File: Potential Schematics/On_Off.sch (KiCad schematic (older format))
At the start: 7 parts

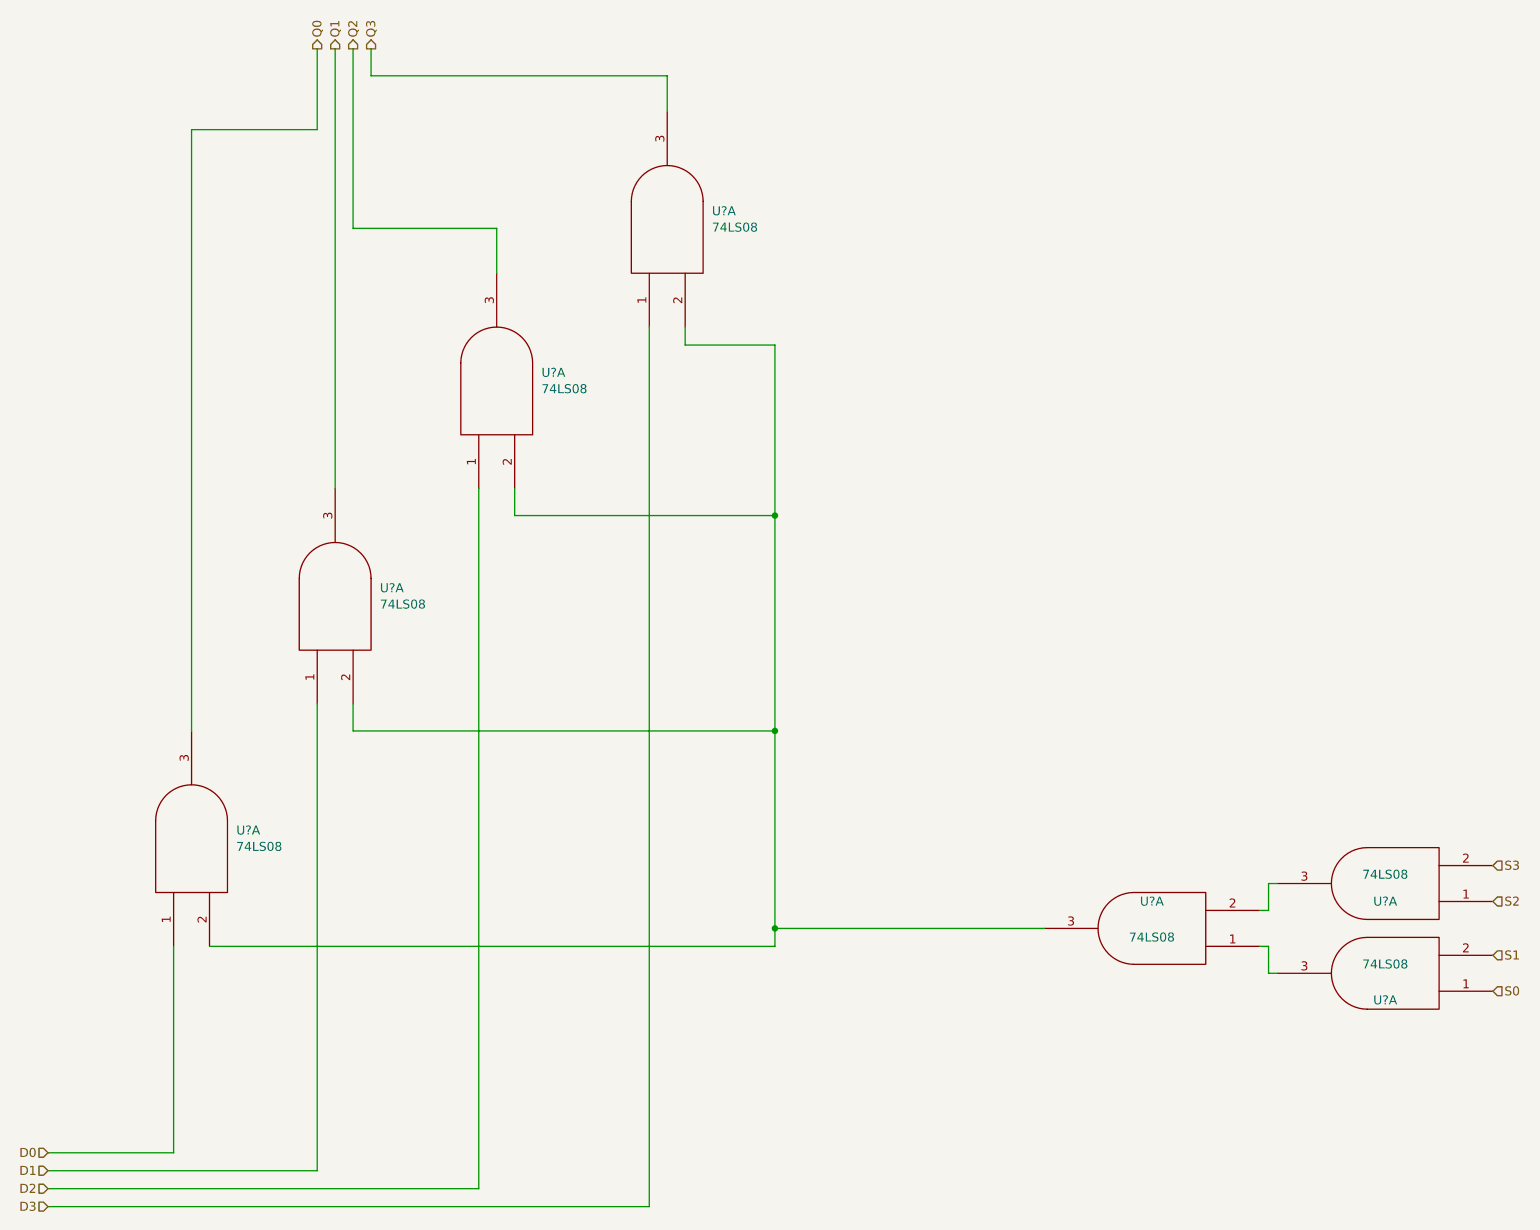
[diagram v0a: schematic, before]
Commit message: Updated overview of Schematic
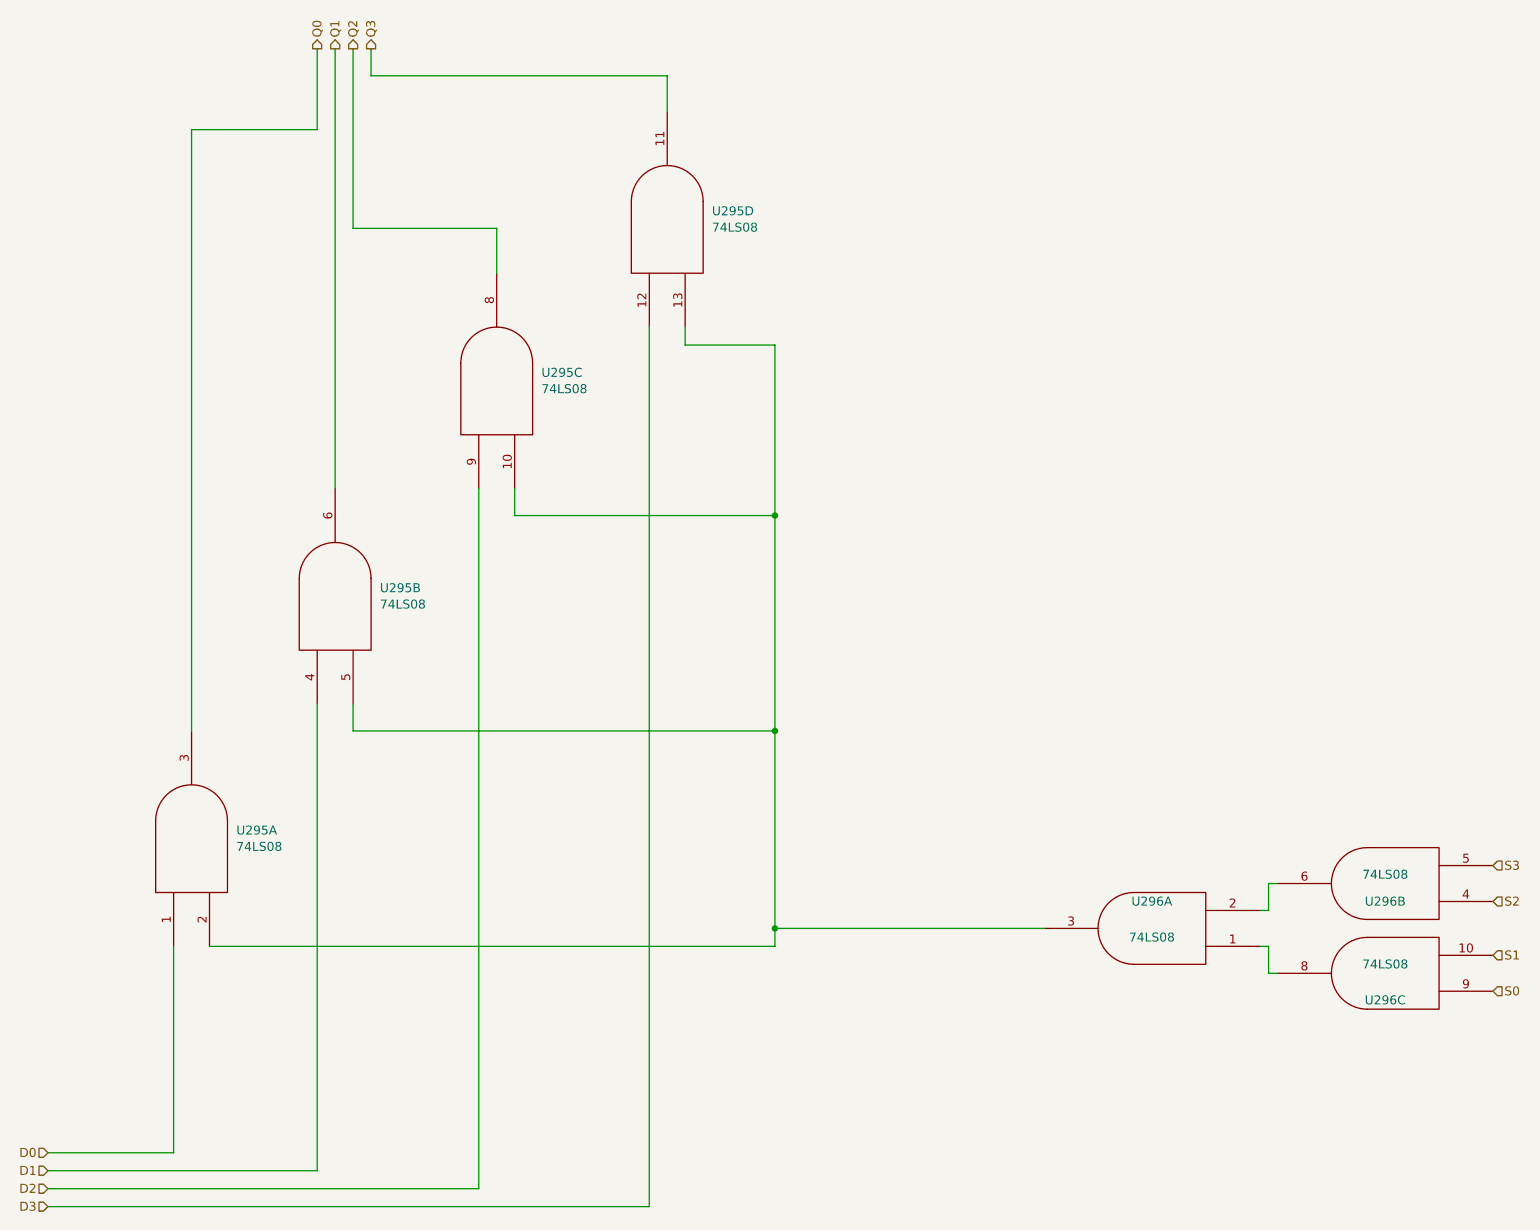
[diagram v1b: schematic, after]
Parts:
- gave numbers to parts that had none: 3
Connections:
- net D1: now also U28.4; no longer U28.1
- net D2: now also U292.9; no longer U292.1
- net D3: now also U292.12; no longer U292.1
- net Q1: now also U28.6; no longer U28.3
- net Q2: now also U292.8; no longer U292.3
- net Q3: now also U292.11; no longer U292.3
- net S0: now also U293.9; no longer U293.1
- net S1: now also U293.10; no longer U293.2
- net S2: now also U292.4; no longer U292.1
- net S3: now also U292.5; no longer U292.2
- net at U292.2: now also U292.6; no longer U292.3
- net at U292.1: now also U293.8; no longer U293.3
- new net: U28.2, U28.5, U292.10, U292.13, U292.3
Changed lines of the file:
@@
 $Descr A4 11693 8268
 encoding utf-8
-Sheet 452 467
+Sheet 452 902
 Title ""
 Date ""
@@
 Q3
 $Comp
-L 4-bit_processor-rescue:74LS08 U?
-U 1 1 5BB2D915
+L 4-bit_processor-rescue:74LS08 U292
+U 2 1 5BB2D915
 P 8900 5700
-F 0 "U?" H 8900 5800 50  0000 C CNN
+AR Path="/5B9D167A/5BAA33A0/5BAA651A/5BB2D6F7/5BB2D915" Ref="U292"  Part="4"
+AR Path="/5B9D167A/5BAA33A0/5BAA651A/5BB302D5/5BB2D915" Ref="U294"  Part="3"
+AR Path="/5B9D167A/5BAA33A0/5BAA651A/5BB303BB/5BB2D915" Ref="U296"  Part="2"
+F 0 "U296" H 8900 5800 50  0000 C CNN
 F 1 "74LS08" H 8900 5650 50  0000 C CNN
 F 2 "" H 8900 5700 50  0001 C CNN
 F 3 "" H 8900 5700 50  0001 C CNN
-	1    8900 5700
+	2    8900 5700
 	-1   0    0    1
 $EndComp
 $Comp
-L 4-bit_processor-rescue:74LS08 U?
-U 1 1 5BB2D984
+L 4-bit_processor-rescue:74LS08 U293
+U 3 1 5BB2D984
 P 8900 6200
-F 0 "U?" H 8900 6350 50  0000 C CNN
+AR Path="/5B9D167A/5BAA33A0/5BAA651A/5BB2D6F7/5BB2D984" Ref="U293"  Part="1"
+AR Path="/5B9D167A/5BAA33A0/5BAA651A/5BB302D5/5BB2D984" Ref="U294"  Part="4"
+AR Path="/5B9D167A/5BAA33A0/5BAA651A/5BB303BB/5BB2D984" Ref="U296"  Part="3"
+F 0 "U296" H 8900 6350 50  0000 C CNN
 F 1 "74LS08" H 8900 6150 50  0000 C CNN
 F 2 "" H 8900 6200 50  0001 C CNN
 F 3 "" H 8900 6200 50  0001 C CNN
-	1    8900 6200
+	3    8900 6200
 	-1   0    0    1
 $EndComp
 $Comp
-L 4-bit_processor-rescue:74LS08 U?
+L 4-bit_processor-rescue:74LS08 U292
 U 1 1 5BB2DA56
 P 7600 5950
-F 0 "U?" H 7600 5800 50  0000 C CNN
+AR Path="/5B9D167A/5BAA33A0/5BAA651A/5BB2D6F7/5BB2DA56" Ref="U292"  Part="3"
+AR Path="/5B9D167A/5BAA33A0/5BAA651A/5BB302D5/5BB2DA56" Ref="U294"  Part="2"
+AR Path="/5B9D167A/5BAA33A0/5BAA651A/5BB303BB/5BB2DA56" Ref="U296"  Part="1"
+F 0 "U296" H 7600 5800 50  0000 C CNN
 F 1 "74LS08" H 7600 6000 50  0000 C CNN
 F 2 "" H 7600 5950 50  0001 C CNN
@@
 	8250 6200 8300 6200
 $Comp
-L 4-bit_processor-rescue:74LS08 U?
+L 4-bit_processor-rescue:74LS08 U28
 U 1 1 5BB2DBA4
 P 2250 5450
-F 0 "U?" V 2296 5201 50  0000 R CNN
+AR Path="/5B9D167A/5BAA33A0/5BAA651A/5BB2D6F7/5BB2DBA4" Ref="U28"  Part="3"
+AR Path="/5B9D167A/5BAA33A0/5BAA651A/5BB302D5/5BB2DBA4" Ref="U293"  Part="2"
+AR Path="/5B9D167A/5BAA33A0/5BAA651A/5BB303BB/5BB2DBA4" Ref="U295"  Part="1"
+F 0 "U295" V 2296 5201 50  0000 R CNN
 F 1 "74LS08" V 2205 5201 50  0000 R CNN
 F 2 "" H 2250 5450 50  0001 C CNN
@@
 $EndComp
 $Comp
-L 4-bit_processor-rescue:74LS08 U?
-U 1 1 5BB2DEAF
+L 4-bit_processor-rescue:74LS08 U28
+U 2 1 5BB2DEAF
 P 3050 4100
-F 0 "U?" V 3096 3851 50  0000 R CNN
+AR Path="/5B9D167A/5BAA33A0/5BAA651A/5BB2D6F7/5BB2DEAF" Ref="U28"  Part="4"
+AR Path="/5B9D167A/5BAA33A0/5BAA651A/5BB302D5/5BB2DEAF" Ref="U293"  Part="3"
+AR Path="/5B9D167A/5BAA33A0/5BAA651A/5BB303BB/5BB2DEAF" Ref="U295"  Part="2"
+F 0 "U295" V 3096 3851 50  0000 R CNN
 F 1 "74LS08" V 3005 3851 50  0000 R CNN
 F 2 "" H 3050 4100 50  0001 C CNN
 F 3 "" H 3050 4100 50  0001 C CNN
-	1    3050 4100
+	2    3050 4100
 	0    -1   -1   0
 $EndComp
 $Comp
-L 4-bit_processor-rescue:74LS08 U?
-U 1 1 5BB2DF82
+L 4-bit_processor-rescue:74LS08 U292
+U 3 1 5BB2DF82
 P 3950 2900
-F 0 "U?" V 3996 2651 50  0000 R CNN
+AR Path="/5B9D167A/5BAA33A0/5BAA651A/5BB2D6F7/5BB2DF82" Ref="U292"  Part="1"
+AR Path="/5B9D167A/5BAA33A0/5BAA651A/5BB302D5/5BB2DF82" Ref="U293"  Part="4"
+AR Path="/5B9D167A/5BAA33A0/5BAA651A/5BB303BB/5BB2DF82" Ref="U295"  Part="3"
+F 0 "U295" V 3996 2651 50  0000 R CNN
 F 1 "74LS08" V 3905 2651 50  0000 R CNN
 F 2 "" H 3950 2900 50  0001 C CNN
 F 3 "" H 3950 2900 50  0001 C CNN
-	1    3950 2900
+	3    3950 2900
 	0    -1   -1   0
 $EndComp
 $Comp
-L 4-bit_processor-rescue:74LS08 U?
-U 1 1 5BB2E032
+L 4-bit_processor-rescue:74LS08 U292
+U 4 1 5BB2E032
 P 4900 2000
-F 0 "U?" V 4946 1751 50  0000 R CNN
+AR Path="/5B9D167A/5BAA33A0/5BAA651A/5BB2D6F7/5BB2E032" Ref="U292"  Part="2"
+AR Path="/5B9D167A/5BAA33A0/5BAA651A/5BB302D5/5BB2E032" Ref="U294"  Part="1"
+AR Path="/5B9D167A/5BAA33A0/5BAA651A/5BB303BB/5BB2E032" Ref="U295"  Part="4"
+F 0 "U295" V 4946 1751 50  0000 R CNN
 F 1 "74LS08" V 4855 1751 50  0000 R CNN
 F 2 "" H 4900 2000 50  0001 C CNN
 F 3 "" H 4900 2000 50  0001 C CNN
-	1    4900 2000
+	4    4900 2000
 	0    -1   -1   0
 $EndComp
